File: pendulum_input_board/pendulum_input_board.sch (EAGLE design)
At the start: 26 parts, among them IC1 FT232H, J1 PJ-051BH, U1 LTC2851MPDDPBF, X1 MINI-USB-UX60-MB-5S8, X2 SM07B-SRSS-TB, X3 SM07B-SRSS-TB

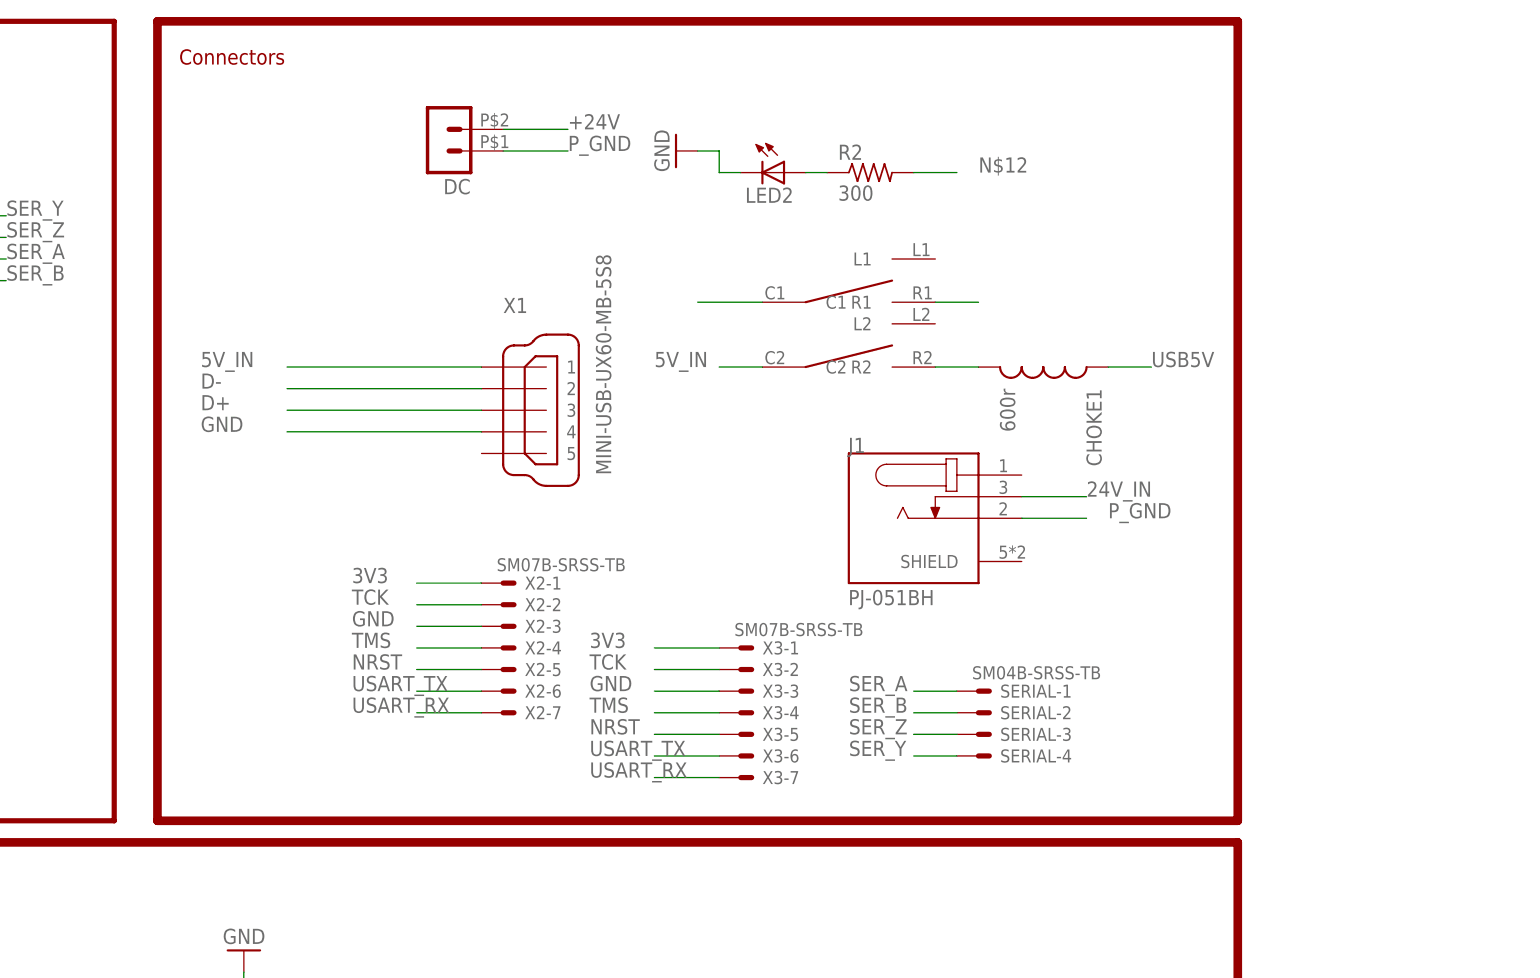
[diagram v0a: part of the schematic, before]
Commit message: Pendulum control demo in python
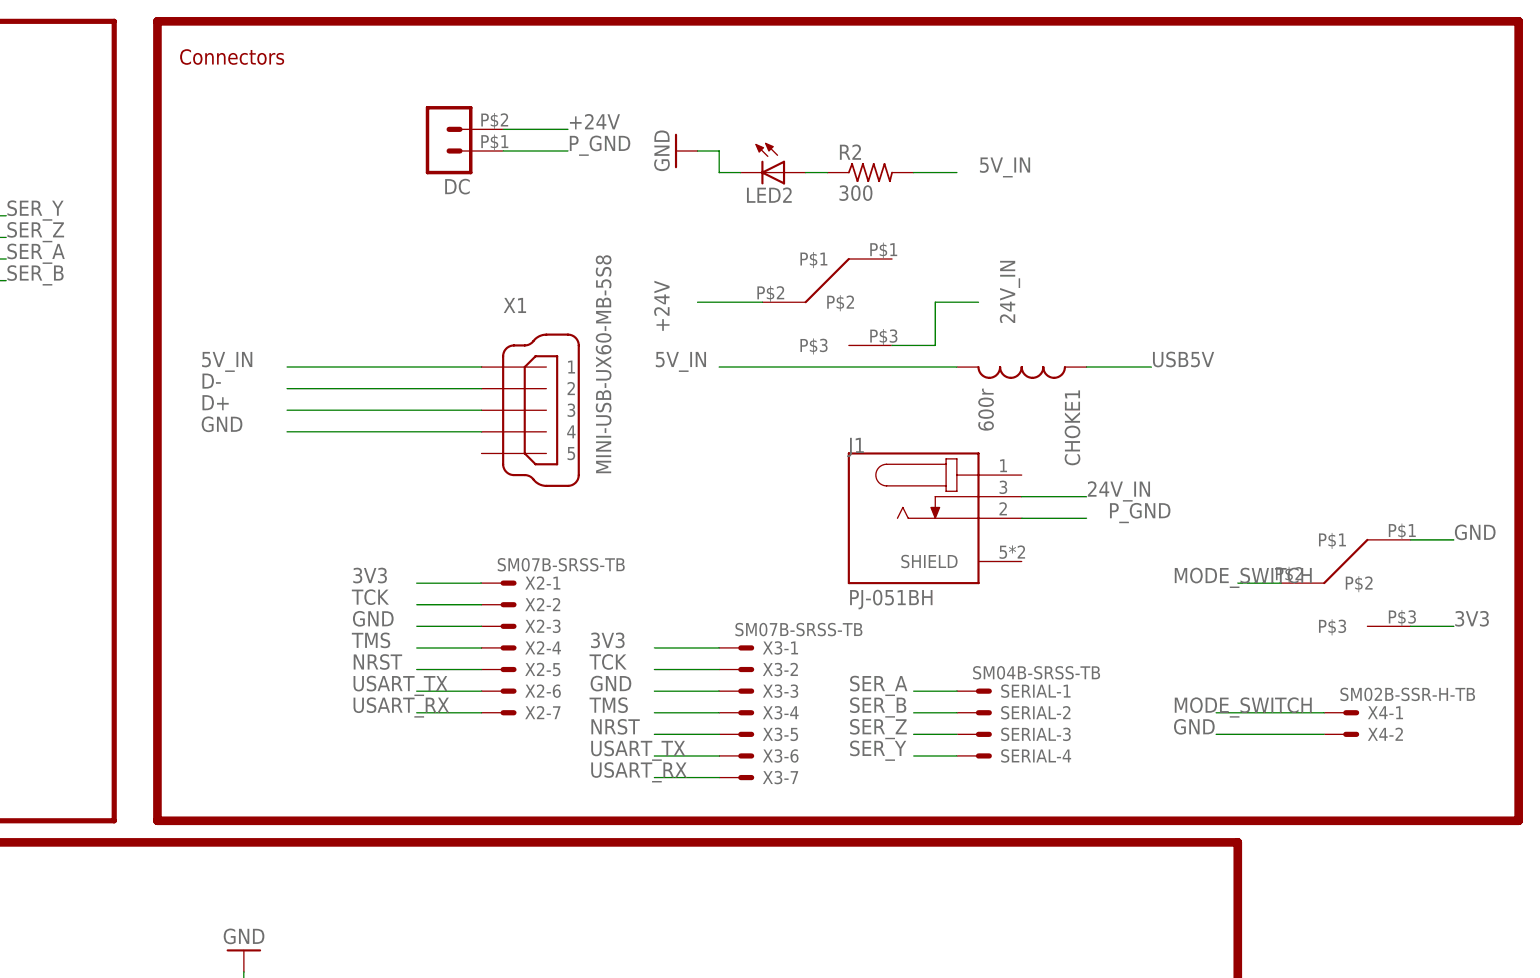
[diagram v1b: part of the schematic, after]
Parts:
- removed U$1: 7201_SWITCH, Ben_Library:7201_SWITCH
- added U$2, U$3: SPDT, Ben_Library:SPDT
- added X4: SM02B-SSR-H-TB, con-jst2:SM02B-SSR-H-TB
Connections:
- removed net N$12: CHOKE1.2, R2.2, U$1.R2
- new net MODE_SWITCH: U$3.P$2, X4-1.S
- net +24V: now also U$2.P$2; no longer U$1.C1
- net 24V_IN: now also U$2.P$3; no longer U$1.R1
- net 3V3: now also U$3.P$3
- net 5V_IN: now also CHOKE1.2, R2.2; no longer U$1.C2
- net GND: now also U$3.P$1, X4-2.S
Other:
- moved on the sheet: CHOKE1
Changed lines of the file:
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@@
 <part name="CHOKE1" library="SparkFun-Passives" deviceset="INDUCTOR" device="0603" value="600r"/>
 <part name="LED2" library="led" deviceset="LED" device="CHIP-LED0603"/>
-<part name="U$1" library="Ben_Library" deviceset="7201_SWITCH" device=""/>
 <part name="R2" library="rcl" deviceset="R-US_" device="R0402" value="300"/>
 <part name="GND10" library="supply1" deviceset="GND" device=""/>
 <part name="X3" library="con-jst2" deviceset="?M07B-SRSS-TB" device="S" value="SM07B-SRSS-TB"/>
 <part name="SERIAL" library="con-jst2" deviceset="?M04B-SRSS-TB" device="S" value="SM04B-SRSS-TB"/>
+<part name="U$2" library="Ben_Library" deviceset="SPDT" device=""/>
+<part name="U$3" library="Ben_Library" deviceset="SPDT" device=""/>
+<part name="X4" library="con-jst2" deviceset="SM02B-SSR-H-TB" device=""/>
 </parts>
 <sheets>
@@
 <wire x1="-55.88" y1="-170.18" x2="-55.88" y2="-5.08" width="1.016" layer="94"/>
 <text x="-48.26" y="-10.16" size="1.778" layer="94">FTDI</text>
-<wire x1="40.64" y1="91.44" x2="167.64" y2="91.44" width="1.016" layer="94"/>
-<wire x1="167.64" y1="91.44" x2="167.64" y2="-2.54" width="1.016" layer="94"/>
-<wire x1="167.64" y1="-2.54" x2="40.64" y2="-2.54" width="1.016" layer="94"/>
+<wire x1="40.64" y1="91.44" x2="200.66" y2="91.44" width="1.016" layer="94"/>
+<wire x1="200.66" y1="91.44" x2="200.66" y2="-2.54" width="1.016" layer="94"/>
+<wire x1="200.66" y1="-2.54" x2="40.64" y2="-2.54" width="1.016" layer="94"/>
 <wire x1="40.64" y1="-2.54" x2="40.64" y2="91.44" width="1.016" layer="94"/>
 <text x="43.18" y="86.36" size="1.778" layer="94">Connectors</text>
@@
 <instance part="C9" gate="G$1" x="43.18" y="-27.94" rot="R180"/>
 <instance part="C10" gate="G$1" x="38.1" y="-27.94" rot="R180"/>
-<instance part="CHOKE1" gate="G$1" x="144.78" y="50.8" rot="R270"/>
+<instance part="CHOKE1" gate="G$1" x="142.24" y="50.8" rot="R270"/>
 <instance part="LED2" gate="G$1" x="114.3" y="73.66" rot="R270"/>
-<instance part="U$1" gate="G$1" x="134.62" y="53.34"/>
 <instance part="R2" gate="G$1" x="124.46" y="73.66"/>
 <instance part="GND10" gate="1" x="101.6" y="76.2" rot="R270"/>
@@
 <instance part="SERIAL" gate="-3" x="137.16" y="7.62"/>
 <instance part="SERIAL" gate="-4" x="137.16" y="5.08"/>
+<instance part="U$2" gate="G$1" x="121.92" y="58.42"/>
+<instance part="U$3" gate="G$1" x="182.88" y="25.4"/>
+<instance part="X4" gate="-1" x="180.34" y="10.16"/>
+<instance part="X4" gate="-2" x="180.34" y="7.62"/>
 </instances>
 <busses>
@@
 <pinref part="X3" gate="-3" pin="S"/>
 </segment>
+<segment>
+<pinref part="X4" gate="-2" pin="S"/>
+<wire x1="177.8" y1="7.62" x2="165.1" y2="7.62" width="0.1524" layer="91"/>
+<label x="160.02" y="7.62" size="1.778" layer="95"/>
+</segment>
+<segment>
+<pinref part="U$3" gate="G$1" pin="P$1"/>
+<wire x1="187.96" y1="30.48" x2="193.04" y2="30.48" width="0.1524" layer="91"/>
+<label x="193.04" y="30.48" size="1.778" layer="95"/>
+</segment>
 </net>
 <net name="+24V" class="0">
@@
 </segment>
 <segment>
-<pinref part="U$1" gate="G$1" pin="C1"/>
 <wire x1="111.76" y1="58.42" x2="104.14" y2="58.42" width="0.1524" layer="91"/>
+<label x="99.06" y="60.96" size="1.778" layer="95" rot="R270"/>
+<pinref part="U$2" gate="G$1" pin="P$2"/>
 </segment>
 </net>
@@
 <label x="91.44" y="17.78" size="1.778" layer="95"/>
 <pinref part="X3" gate="-1" pin="S"/>
+</segment>
+<segment>
+<pinref part="U$3" gate="G$1" pin="P$3"/>
+<wire x1="187.96" y1="20.32" x2="193.04" y2="20.32" width="0.1524" layer="91"/>
+<label x="193.04" y="20.32" size="1.778" layer="95"/>
 </segment>
 </net>
@@
 <segment>
 <pinref part="CHOKE1" gate="G$1" pin="1"/>
-<wire x1="152.4" y1="50.8" x2="157.48" y2="50.8" width="0.1524" layer="91"/>
+<wire x1="149.86" y1="50.8" x2="157.48" y2="50.8" width="0.1524" layer="91"/>
 <label x="157.48" y="50.8" size="1.778" layer="95"/>
 </segment>
@@
 </segment>
 <segment>
-<pinref part="U$1" gate="G$1" pin="R1"/>
 <wire x1="132.08" y1="58.42" x2="137.16" y2="58.42" width="0.1524" layer="91"/>
+<label x="139.7" y="63.5" size="1.778" layer="95" rot="R270"/>
+<pinref part="U$2" gate="G$1" pin="P$3"/>
+<wire x1="127" y1="53.34" x2="132.08" y2="53.34" width="0.1524" layer="91"/>
+<wire x1="132.08" y1="53.34" x2="132.08" y2="58.42" width="0.1524" layer="91"/>
 </segment>
 </net>
@@
 </segment>
 <segment>
-<pinref part="U$1" gate="G$1" pin="C2"/>
-<wire x1="111.76" y1="50.8" x2="106.68" y2="50.8" width="0.1524" layer="91"/>
+<wire x1="134.62" y1="50.8" x2="106.68" y2="50.8" width="0.1524" layer="91"/>
 <label x="99.06" y="50.8" size="1.778" layer="95"/>
-</segment>
-</net>
-<net name="N$12" class="0">
-<segment>
 <pinref part="CHOKE1" gate="G$1" pin="2"/>
-<pinref part="U$1" gate="G$1" pin="R2"/>
-<wire x1="137.16" y1="50.8" x2="132.08" y2="50.8" width="0.1524" layer="91"/>
 </segment>
 <segment>
@@
 </segment>
 </net>
+<net name="MODE_SWITCH" class="0">
+<segment>
+<pinref part="X4" gate="-1" pin="S"/>
+<wire x1="177.8" y1="10.16" x2="165.1" y2="10.16" width="0.1524" layer="91"/>
+<label x="160.02" y="10.16" size="1.778" layer="95"/>
+</segment>
+<segment>
+<pinref part="U$3" gate="G$1" pin="P$2"/>
+<wire x1="172.72" y1="25.4" x2="167.64" y2="25.4" width="0.1524" layer="91"/>
+<label x="160.02" y="25.4" size="1.778" layer="95"/>
+</segment>
+</net>

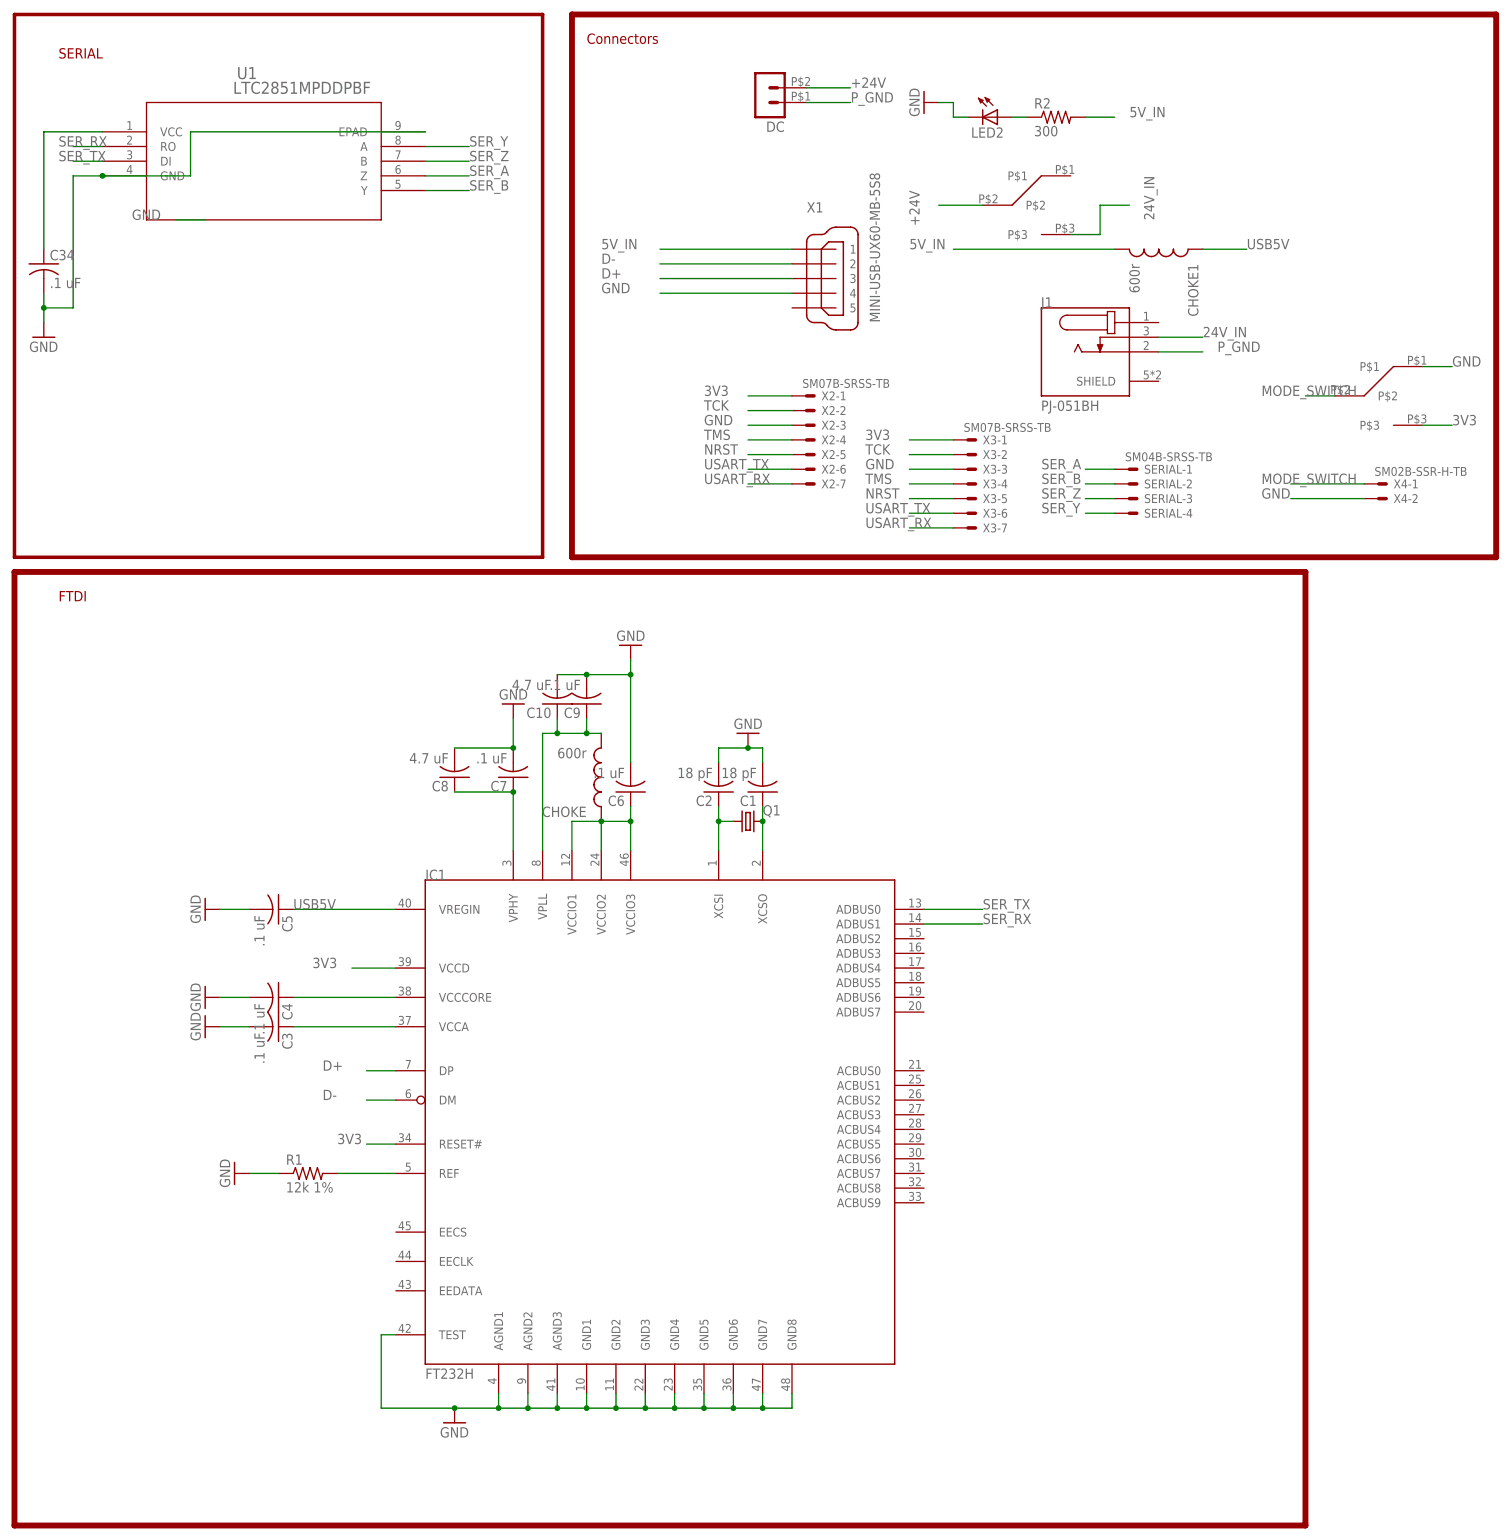
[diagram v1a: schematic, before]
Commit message: updated pendulum software
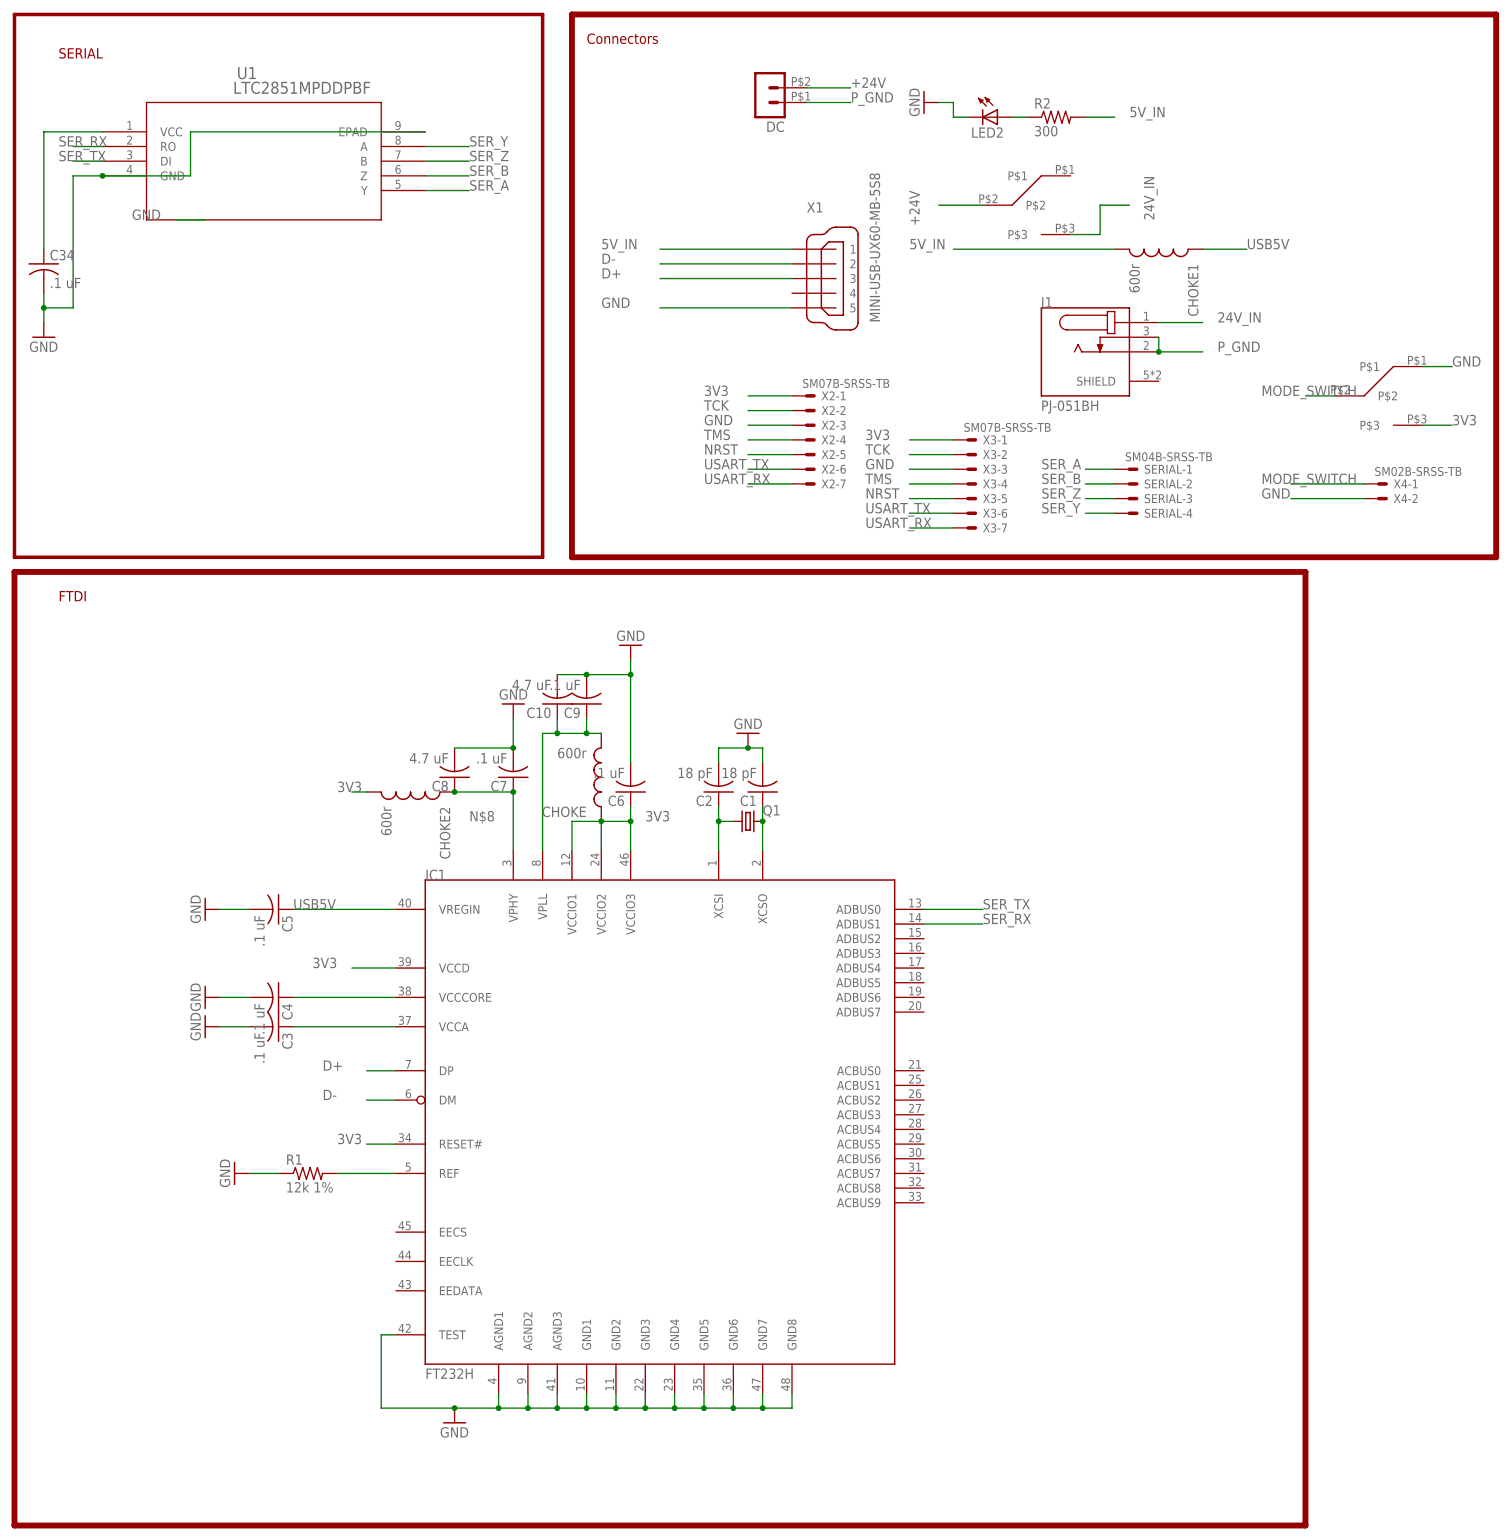
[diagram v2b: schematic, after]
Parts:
- added CHOKE2: 600r, SparkFun-Passives:INDUCTOR0603
- X4: value SM02B-SSR-H-TB -> SM02B-SRSS-TB; device con-jst2:SM02B-SSR-H-TB -> con-jst2:SM02B-SRSS-TB
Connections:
- removed net 3V1: C34.1, U1.VCC
- removed net N$7: C6.1, CHOKE.1, IC1.VCCIO1, IC1.VCCIO2, IC1.VCCIO3
- net 24V_IN: now also J1.1; no longer J1.3
- net 3V3: now also C34.1, C6.1, CHOKE.1, CHOKE2.2, IC1.VCCIO1, IC1.VCCIO2, IC1.VCCIO3, U1.VCC
- net GND: now also X1.5; no longer X1.4
- net N$8: now also CHOKE2.1
- net P_GND: now also J1.3
- net SER_A: now also U1.Y; no longer U1.Z
- net SER_B: now also U1.Z; no longer U1.Y
